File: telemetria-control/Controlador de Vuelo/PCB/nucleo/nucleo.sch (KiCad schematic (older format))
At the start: 8 parts, among them P1 CONN_4, P2 DIL16, P3 CONN_2, P4 CONN_4, U1 4051

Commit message: esquemático modificado
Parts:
- removed P1, P4: CONN_4, symbol CONN_4
- removed P2: DIL16, symbol DIL16
- removed P3: CONN_2, symbol CONN_2
- removed U1: 4051, symbol 4051
- added C1: 100nF, symbol C
- added D1: D, symbol D
- added P1: POWER, symbol CONN_01X02
- added P2: UART, symbol CONN_01X03
- added P3, P4: CONN_01X07, symbol CONN_01X07
- added R1: 12K, ~, symbol R
- added R10, R3: 4.7K, ~, symbol R
- added R2, R4: 470, ~, symbol R
- added R5, R6, R8: 4.7K, symbol R
- added R7: 220K, symbol R
- added R9: 100K, symbol R
- added SW1: RST, symbol push_button
- added SW2: FLASH, symbol push_button
- added U2: 4051, symbol 4051
- R11: renamed from R1; value R -> 4.7K
- R12: renamed from R2; value R -> 4.7K
- R13: renamed from R3; value R -> 4.7K
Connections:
- net labels added: +3.3V, ->Tx, <-Rx, ESP07, FLASH, RST
- net labels removed: A, Ac 1, Ac 2, Adc, B, C, Rx0, Tx0, VCC
- wire segments 35 -> 121
- no-connect marks 14 -> 2
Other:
- note added: "Circuito de Flash"
- note added: "Circuito de Reset"
- note added: "Pullup I2C\n"
- moved on the sheet: R11, R12, R13

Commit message: agregados capacitores de desacople
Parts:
- added C2: 100nF, symbol C
- added C3: 47uF, symbol CP
- P3: value CONN_01X07 -> SENSOR_BOARD_1
- P4: value CONN_01X07 -> SENSOR_BOARD_2
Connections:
- net +3V3: now also C2.2, C3.1
- net GND: now also C2.1, C3.2
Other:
- moved on the sheet: R7, R8, R9

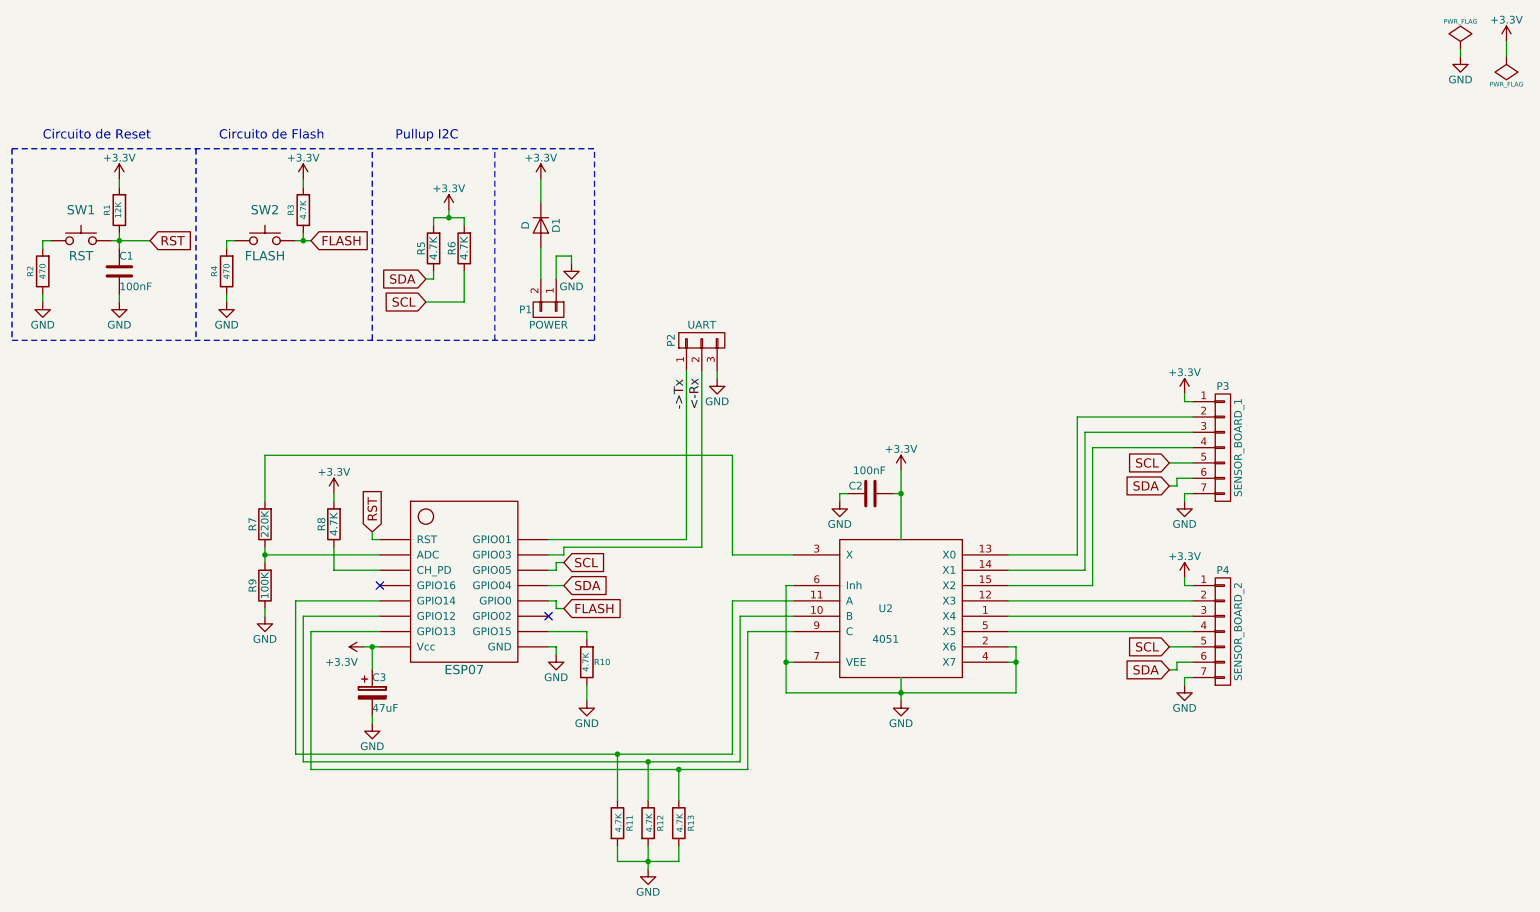
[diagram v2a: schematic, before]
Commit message: agrego componentes smd en la netlist
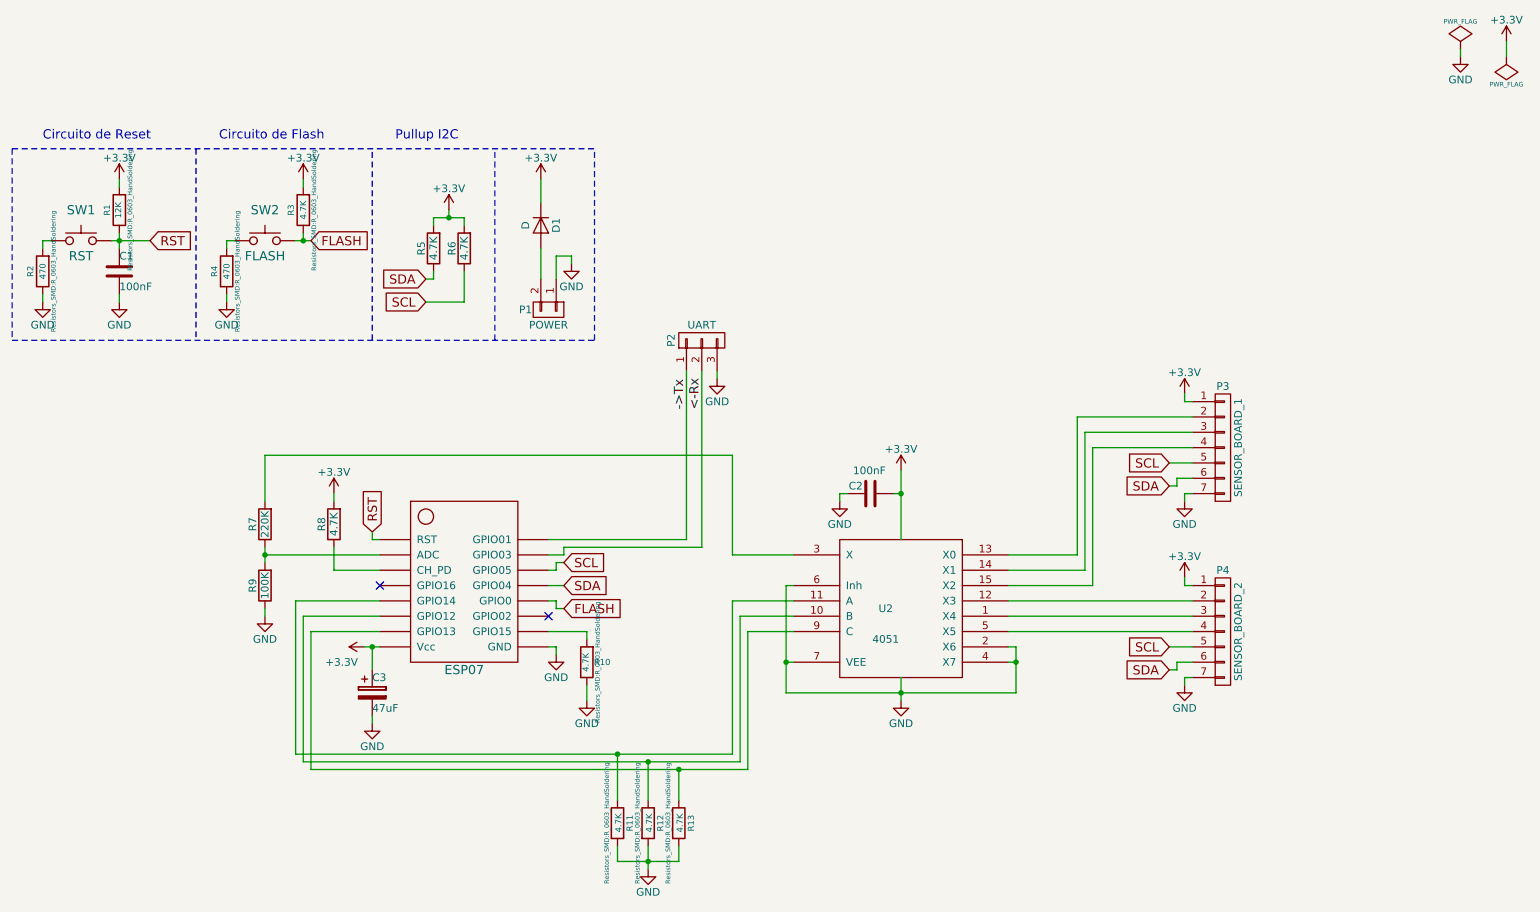
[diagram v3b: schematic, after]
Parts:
- C1, C2, C3: footprint (none) -> Capacitors_SMD:C_0603_HandSoldering
- D1: footprint (none) -> Diodes_SMD:D_0603
- P1: footprint (none) -> Connectors_Terminal_Blocks:TerminalBlock_Pheonix_MPT-2.54mm_2pol
- P2: footprint (none) -> Connectors_Terminal_Blocks:TerminalBlock_Pheonix_MPT-2.54mm_3pol
- P3, P4: footprint (none) -> Connectors_Terminal_Blocks:TerminalBlock_Pheonix_MPT-2.54mm_7pol
- R1, R10, R11, R12, R13, R2, R3, R4: footprint ~ -> Resistors_SMD:R_0603_HandSoldering
- R5, R6, R7, R8, R9: footprint (none) -> Resistors_SMD:R_0603_HandSoldering
- SW1, SW2: footprint (none) -> Buttons_Switches_SMD:SW_SPST_TL3342
- U2: footprint (none) -> Housings_DIP:DIP-16_W7.62mm_LongPads
